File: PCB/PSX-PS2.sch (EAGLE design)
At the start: 21 parts, among them U1A SN74AHCT125N, U2A SN74AHCT125N, U3A SN74AHCT125N, U4A SN74AHCT125N

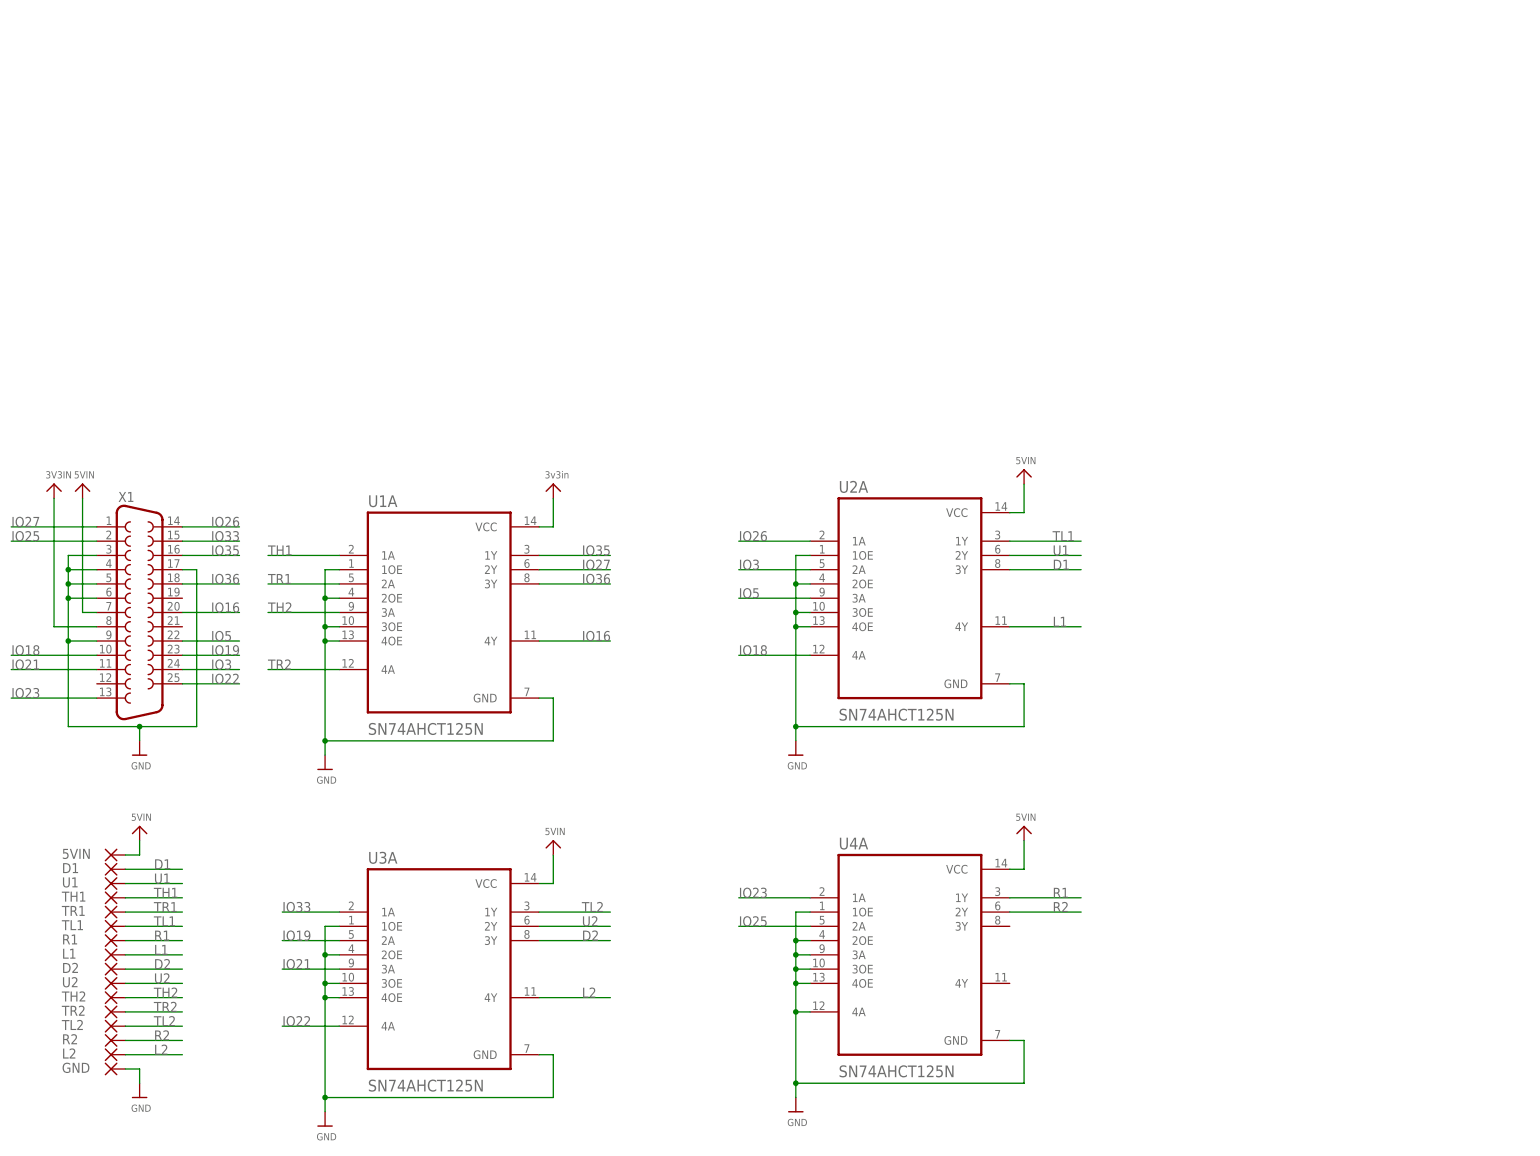
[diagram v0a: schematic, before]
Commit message: PCB Updates/New Additions
All existing PCBs had silkscreen updates and NES, Virtual Boy, PSX/PS2, Nintendo 64, Saturn have been added.
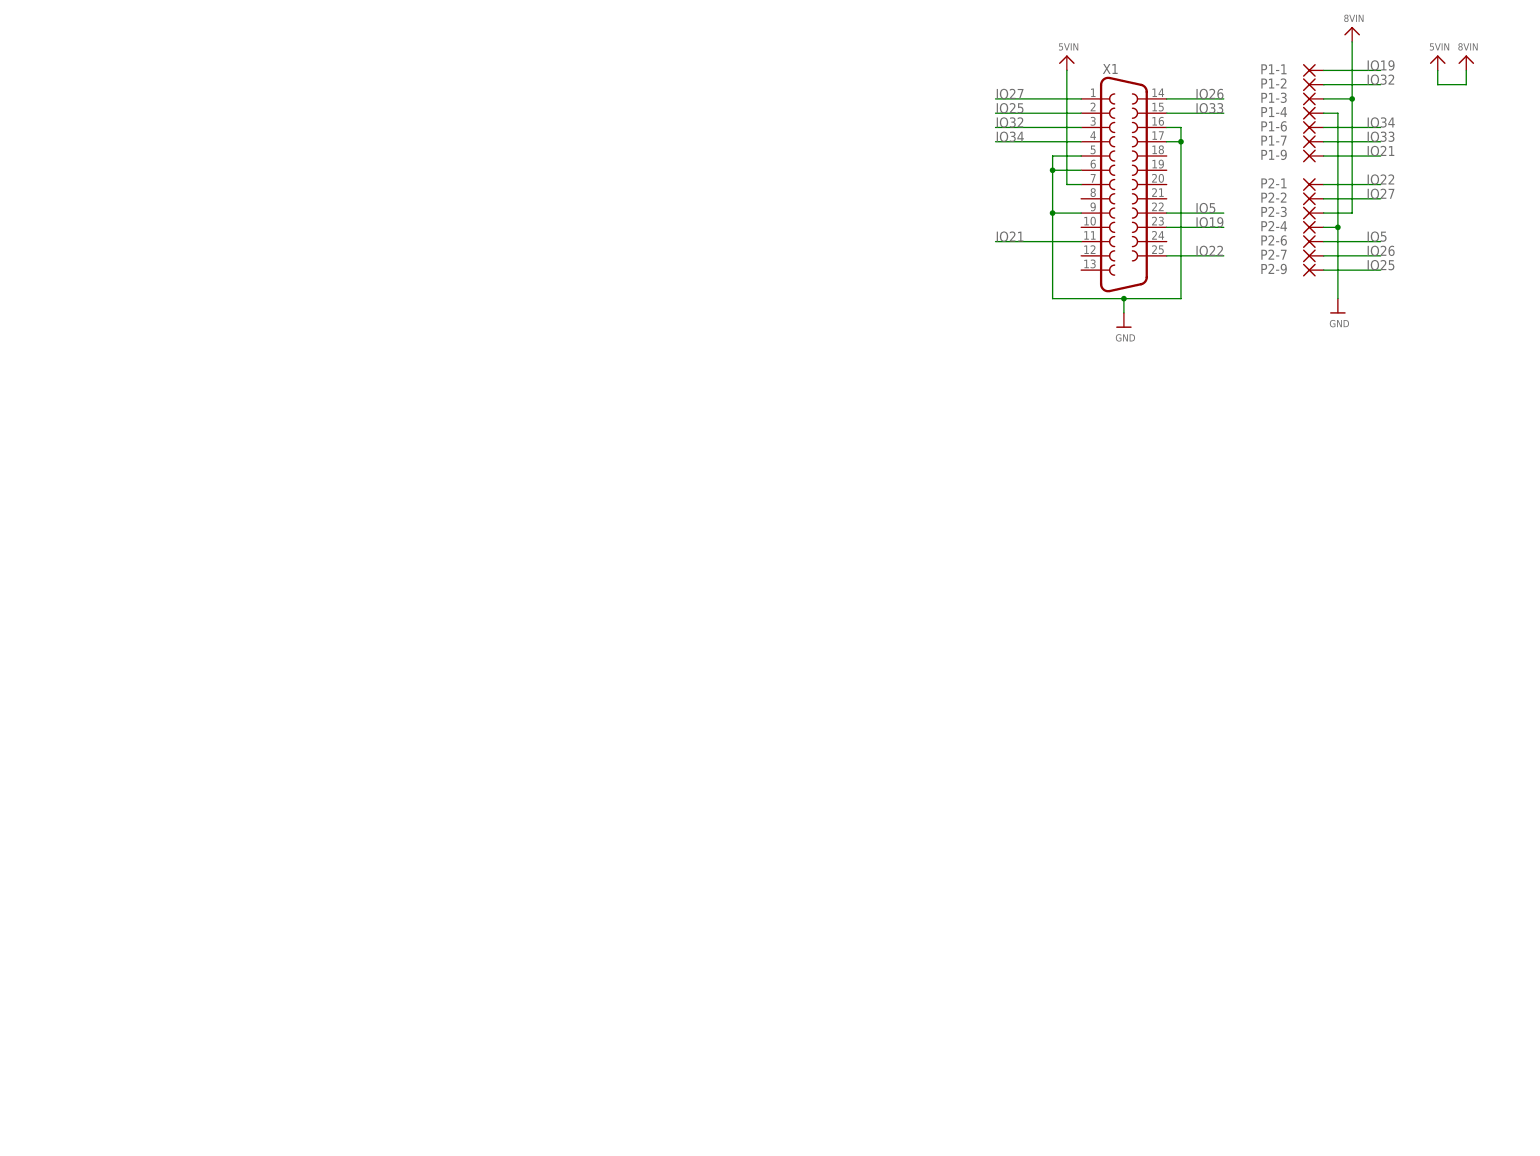
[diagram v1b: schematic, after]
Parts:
- removed 5VIN, D1, D2, GND, L1, L2, R1, R2, TH1, TH2, TL1, TL2, TR1, TR2, U1, U2: (no value), wirepad:SMD5
- removed U1A, U2A, U3A, U4A: SN74AHCT125N, SN74AHCT125N:SN74AHCT125N
- added P1-1, P1-2, P1-3, P1-4, P1-6, P1-7, P1-9, P2-1, P2-2, P2-3, P2-4, P2-6, P2-7, P2-9: (no value), wirepad:SMD5
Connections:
- removed net 3V3IN: U1A.VCC, X1.8
- removed net D1: D1.P, U2A.3Y
- removed net D2: D2.P, U3A.3Y
- removed net IO16: U1A.4Y, X1.20
- removed net IO18: U2A.4A, X1.10
- removed net IO23: U4A.1A, X1.13
- removed net IO3: U2A.2A, X1.24
- removed net IO35: U1A.1Y, X1.16
- removed net IO36: U1A.3Y, X1.18
- removed net L1: L1.P, U2A.4Y
- removed net L2: L2.P, U3A.4Y
- removed net R1: R1.P, U4A.1Y
- removed net R2: R2.P, U4A.2Y
- removed net TH1: TH1.P, U1A.1A
- removed net TH2: TH2.P, U1A.3A
- removed net TL1: TL1.P, U2A.1Y
- removed net TL2: TL2.P, U3A.1Y
- removed net TR1: TR1.P, U1A.2A
- removed net TR2: TR2.P, U1A.4A
- removed net U1: U1.P, U2A.2Y
- removed net U2: U2.P, U3A.2Y
- new net IO32: P1-2.P, X1.3
- new net IO34: P1-6.P, X1.4
- net 5VIN: now also P1-3.P, P2-3.P; no longer 5VIN.P, U2A.VCC, U3A.VCC, U4A.VCC
- net GND: now also P1-4.P, P2-4.P, X1.16; no longer GND.P, U1A.1OE, U1A.2OE, U1A.3OE, U1A.4OE, U1A.GND, U2A.1OE, U2A.2OE, U2A.3OE, U2A.4OE, U2A.GND, U3A.1OE, U3A.2OE, U3A.3OE, U3A.4OE, U3A.GND, U4A.1OE, U4A.2OE, U4A.3A, U4A.3OE, U4A.4A, U4A.4OE, U4A.GND, X1.3, X1.4
- net IO19: now also P1-1.P; no longer U3A.2A
- net IO21: now also P1-9.P; no longer U3A.3A
- net IO22: now also P2-1.P; no longer U3A.4A
- net IO25: now also P2-9.P; no longer U4A.2A
- net IO26: now also P2-7.P; no longer U2A.1A
- net IO27: now also P2-2.P; no longer U1A.2Y
- net IO33: now also P1-7.P; no longer U3A.1A
- net IO5: now also P2-6.P; no longer U2A.3A
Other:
- moved on the sheet: X1

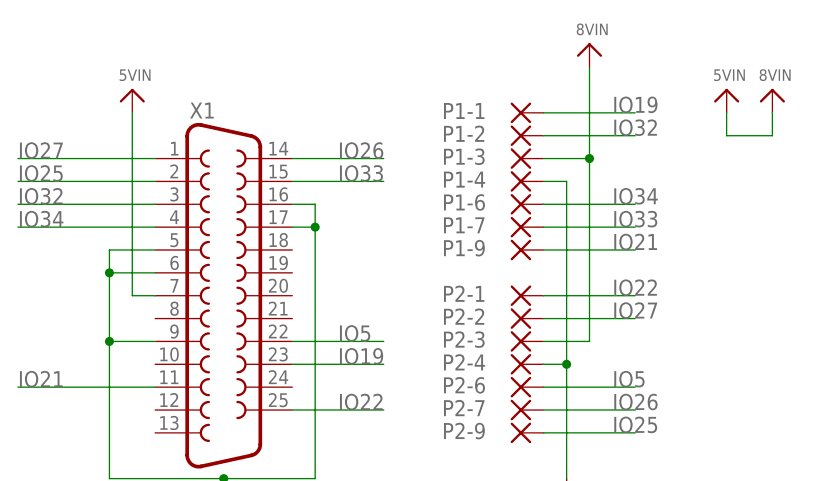
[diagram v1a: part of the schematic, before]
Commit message: PS2 Power Pin Swap
The PCB could not detect the correct system using the 8V from the PS2 to the 5VIN on the ESP.  Moving to the 3V3 from the PS2 to 3V3IN on the ESP corrected the issue and the PCB not works as intended.
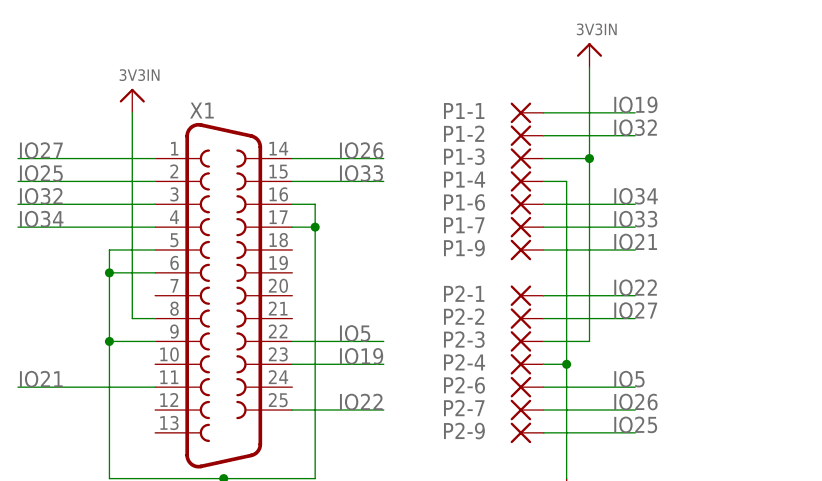
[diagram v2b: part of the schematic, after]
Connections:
- removed net 5VIN: P1-3.P, P2-3.P, X1.7
- new net 3V3IN: P1-3.P, P2-3.P, X1.8

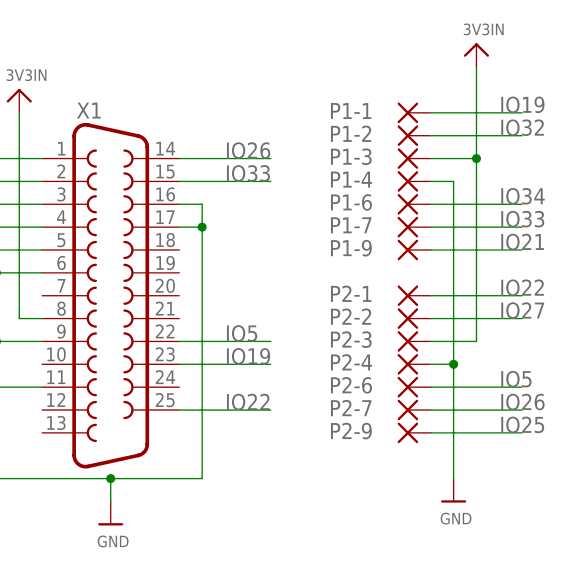
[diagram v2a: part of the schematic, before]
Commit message: Updated Pad Name for 3V3 input
Pad name was still listed as P1-4/P2-4 which is the 8V pin, The pads have been renamed and order updated on the PCB
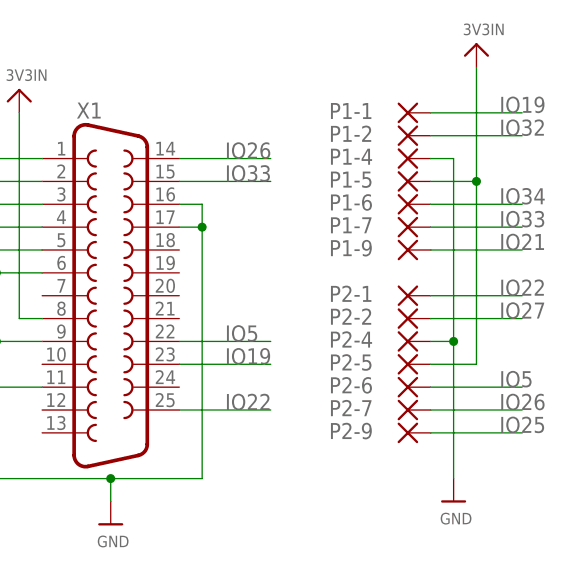
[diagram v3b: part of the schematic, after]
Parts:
- removed P1-3, P2-3: (no value), wirepad:SMD5
- added P1-5, P2-5: (no value), wirepad:SMD5
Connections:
- net 3V3IN: now also P1-5.P, P2-5.P; no longer P1-3.P, P2-3.P
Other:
- moved on the sheet: P1-4, P2-4
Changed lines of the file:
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@@
 <part name="U$53" library="microbuilder" deviceset="VIN" device="" value="3V3IN"/>
 <part name="U$54" library="Airquality_Sensor" library_urn="urn:adsk.eagle:library:16015176" deviceset="GND" device=""/>
-<part name="P1-3" library="wirepad" library_urn="urn:adsk.eagle:library:412" deviceset="SMD5" device="" package3d_urn="urn:adsk.eagle:package:30841/1"/>
+<part name="P1-5" library="wirepad" library_urn="urn:adsk.eagle:library:412" deviceset="SMD5" device="" package3d_urn="urn:adsk.eagle:package:30841/1"/>
 <part name="P2-2" library="wirepad" library_urn="urn:adsk.eagle:library:412" deviceset="SMD5" device="" package3d_urn="urn:adsk.eagle:package:30841/1"/>
 <part name="P1-6" library="wirepad" library_urn="urn:adsk.eagle:library:412" deviceset="SMD5" device="" package3d_urn="urn:adsk.eagle:package:30841/1"/>
@@
 <part name="P1-9" library="wirepad" library_urn="urn:adsk.eagle:library:412" deviceset="SMD5" device="" package3d_urn="urn:adsk.eagle:package:30841/1"/>
 <part name="P2-1" library="wirepad" library_urn="urn:adsk.eagle:library:412" deviceset="SMD5" device="" package3d_urn="urn:adsk.eagle:package:30841/1"/>
-<part name="P2-3" library="wirepad" library_urn="urn:adsk.eagle:library:412" deviceset="SMD5" device="" package3d_urn="urn:adsk.eagle:package:30841/1"/>
+<part name="P2-5" library="wirepad" library_urn="urn:adsk.eagle:library:412" deviceset="SMD5" device="" package3d_urn="urn:adsk.eagle:package:30841/1"/>
 <part name="P2-4" library="wirepad" library_urn="urn:adsk.eagle:library:412" deviceset="SMD5" device="" package3d_urn="urn:adsk.eagle:package:30841/1"/>
 <part name="P2-6" library="wirepad" library_urn="urn:adsk.eagle:library:412" deviceset="SMD5" device="" package3d_urn="urn:adsk.eagle:package:30841/1"/>
@@
 <attribute name="VALUE" x="412.496" y="-40.64" size="1.27" layer="96"/>
 </instance>
-<instance part="P1-3" gate="1" x="447.04" y="2.54" smashed="yes">
-<attribute name="NAME" x="438.277" y="1.8542" size="1.778" layer="95"/>
-<attribute name="VALUE" x="445.897" y="-0.762" size="1.778" layer="96"/>
+<instance part="P1-5" gate="1" x="447.04" y="0" smashed="yes">
+<attribute name="NAME" x="438.277" y="-0.6858" size="1.778" layer="95"/>
+<attribute name="VALUE" x="445.897" y="-3.302" size="1.778" layer="96"/>
 </instance>
 <instance part="P2-2" gate="1" x="447.04" y="-15.24" smashed="yes">
@@
 <attribute name="VALUE" x="445.897" y="-5.842" size="1.778" layer="96"/>
 </instance>
-<instance part="P1-4" gate="1" x="447.04" y="0" smashed="yes">
-<attribute name="NAME" x="438.277" y="-0.6858" size="1.778" layer="95"/>
-<attribute name="VALUE" x="445.897" y="-3.302" size="1.778" layer="96"/>
+<instance part="P1-4" gate="1" x="447.04" y="2.54" smashed="yes">
+<attribute name="NAME" x="438.277" y="1.8542" size="1.778" layer="95"/>
+<attribute name="VALUE" x="445.897" y="-0.762" size="1.778" layer="96"/>
 </instance>
 <instance part="P1-7" gate="1" x="447.04" y="-5.08" smashed="yes">
@@
 <attribute name="VALUE" x="445.897" y="-16.002" size="1.778" layer="96"/>
 </instance>
-<instance part="P2-3" gate="1" x="447.04" y="-17.78" smashed="yes">
+<instance part="P2-5" gate="1" x="447.04" y="-20.32" smashed="yes">
+<attribute name="NAME" x="438.277" y="-21.0058" size="1.778" layer="95"/>
+<attribute name="VALUE" x="445.897" y="-23.622" size="1.778" layer="96"/>
+</instance>
+<instance part="P2-4" gate="1" x="447.04" y="-17.78" smashed="yes">
 <attribute name="NAME" x="438.277" y="-18.4658" size="1.778" layer="95"/>
 <attribute name="VALUE" x="445.897" y="-21.082" size="1.778" layer="96"/>
-</instance>
-<instance part="P2-4" gate="1" x="447.04" y="-20.32" smashed="yes">
-<attribute name="NAME" x="438.277" y="-21.0058" size="1.778" layer="95"/>
-<attribute name="VALUE" x="445.897" y="-23.622" size="1.778" layer="96"/>
 </instance>
 <instance part="P2-6" gate="1" x="447.04" y="-22.86" smashed="yes">
@@
 <segment>
 <pinref part="P1-4" gate="1" pin="P"/>
-<wire x1="449.58" y1="0" x2="452.12" y2="0" width="0.1524" layer="91"/>
+<wire x1="449.58" y1="2.54" x2="452.12" y2="2.54" width="0.1524" layer="91"/>
 <pinref part="U$52" gate="G$1" pin="GND"/>
-<wire x1="452.12" y1="0" x2="452.12" y2="-20.32" width="0.1524" layer="91"/>
+<wire x1="452.12" y1="2.54" x2="452.12" y2="-17.78" width="0.1524" layer="91"/>
 <pinref part="P2-4" gate="1" pin="P"/>
-<wire x1="452.12" y1="-20.32" x2="452.12" y2="-33.02" width="0.1524" layer="91"/>
-<wire x1="449.58" y1="-20.32" x2="452.12" y2="-20.32" width="0.1524" layer="91"/>
-<junction x="452.12" y="-20.32"/>
+<wire x1="452.12" y1="-17.78" x2="452.12" y2="-33.02" width="0.1524" layer="91"/>
+<wire x1="449.58" y1="-17.78" x2="452.12" y2="-17.78" width="0.1524" layer="91"/>
+<junction x="452.12" y="-17.78"/>
 </segment>
 </net>
@@
 </segment>
 <segment>
-<pinref part="P1-3" gate="1" pin="P"/>
-<wire x1="449.58" y1="2.54" x2="454.66" y2="2.54" width="0.1524" layer="91"/>
+<pinref part="P1-5" gate="1" pin="P"/>
+<wire x1="449.58" y1="0" x2="454.66" y2="0" width="0.1524" layer="91"/>
 <pinref part="U$55" gate="G$1" pin="VIN"/>
-<wire x1="454.66" y1="2.54" x2="454.66" y2="12.7" width="0.1524" layer="91"/>
-<pinref part="P2-3" gate="1" pin="P"/>
-<wire x1="449.58" y1="-17.78" x2="454.66" y2="-17.78" width="0.1524" layer="91"/>
-<wire x1="454.66" y1="-17.78" x2="454.66" y2="2.54" width="0.1524" layer="91"/>
-<junction x="454.66" y="2.54"/>
-</segment>
-</net>
+<wire x1="454.66" y1="0" x2="454.66" y2="12.7" width="0.1524" layer="91"/>
+<pinref part="P2-5" gate="1" pin="P"/>
+<wire x1="449.58" y1="-20.32" x2="454.66" y2="-20.32" width="0.1524" layer="91"/>
+<wire x1="454.66" y1="-20.32" x2="454.66" y2="0" width="0.1524" layer="91"/>
+<junction x="454.66" y="0"/>
+</segment>
+</net>

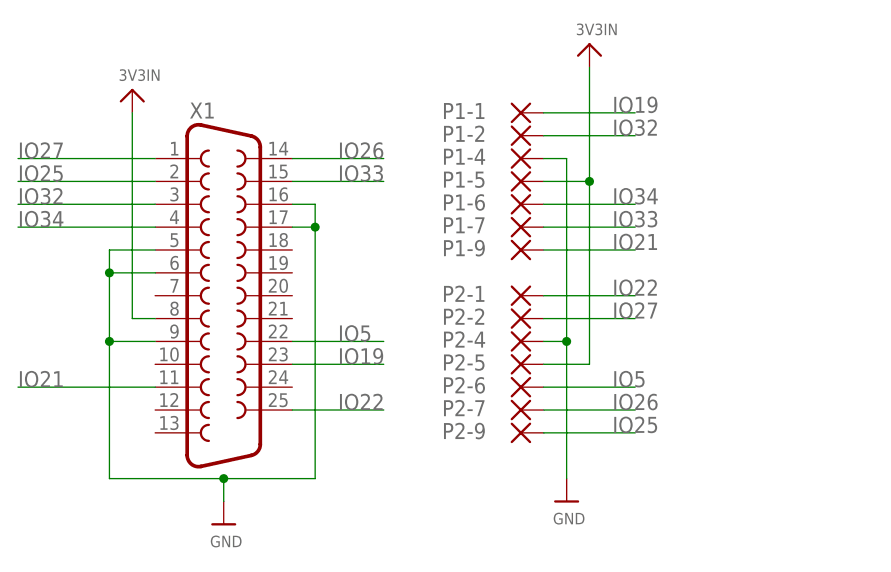
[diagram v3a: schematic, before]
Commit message: Power Pin addition
After working with Darthcloud, it was revealed that some PS2 consoles have weak VIN on either the 8V or the 3V3.  To make sure this PCB will work in either situation, I have added the 8V (Pad 3) pad back on to the PCB in addition to the 3V3 Pad (Pad 5).  Only one needs to be used to power the ESP.
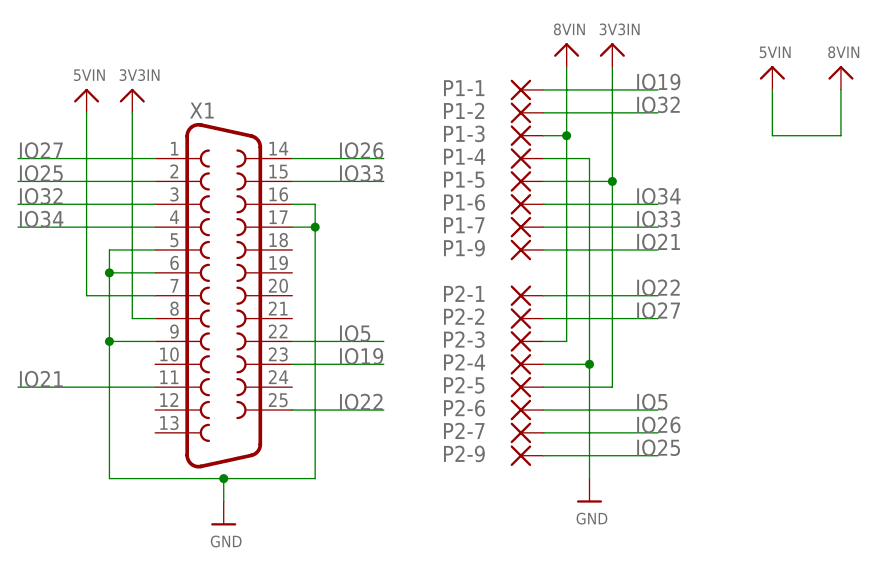
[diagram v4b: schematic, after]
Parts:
- added P1-3, P2-3: (no value), wirepad:SMD5
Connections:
- new net VIN: P1-3.P, P2-3.P, X1.7
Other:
- moved on the sheet: P1-1, P1-2, P2-4, P2-5, P2-6, P2-7, P2-9
